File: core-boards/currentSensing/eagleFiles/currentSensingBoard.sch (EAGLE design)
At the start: 22 parts, among them Q1 16MHz

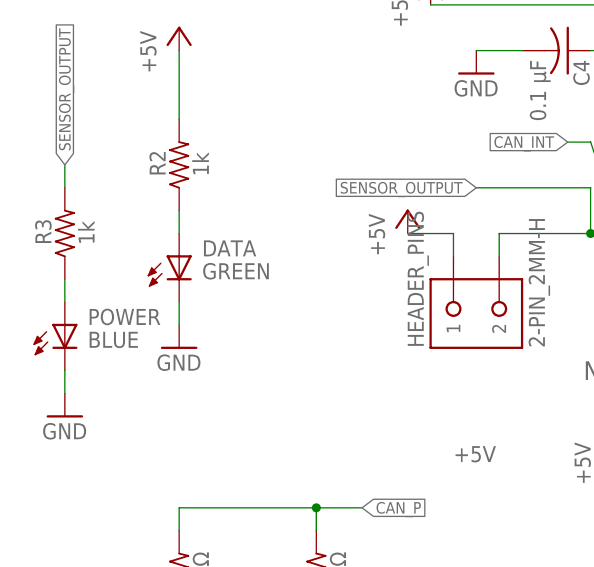
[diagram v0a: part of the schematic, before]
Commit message: Leds fixed
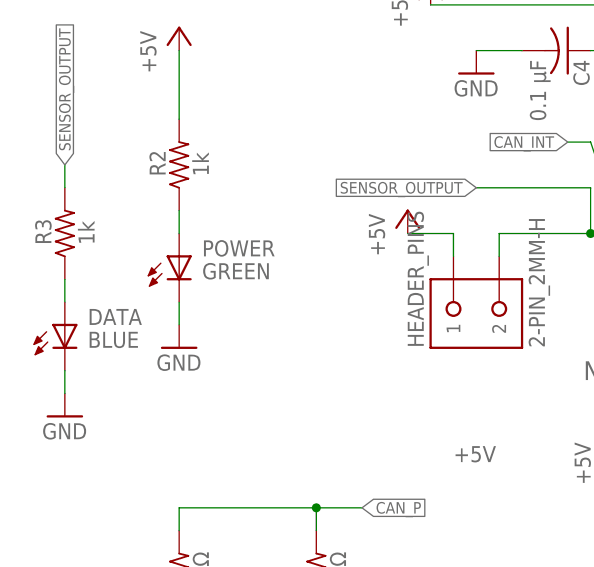
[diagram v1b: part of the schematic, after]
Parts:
- DATA: value GREEN -> BLUE; device RoboJackets-LEDs:LED-SMD-GREEN -> RoboJackets-LEDs:LED-SMD-BLUE
- POWER: value BLUE -> GREEN; device RoboJackets-LEDs:LED-SMD-BLUE -> RoboJackets-LEDs:LED-SMD-GREEN
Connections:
- net N$2: now also DATA.A; no longer POWER.A
- net N$7: now also POWER.A; no longer DATA.A
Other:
- moved on the sheet: DATA, POWER
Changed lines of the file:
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@@
 <part name="P+10" library="supply1" library_urn="urn:adsk.eagle:library:371" deviceset="+5V" device=""/>
 <part name="HEADER_PINS" library="RoboJackets-Connectors" deviceset="2-PIN_2MM-*" device="H"/>
-<part name="DATA" library="RoboJackets-LEDs" deviceset="LED-SMD" device="" technology="-GREEN" value="GREEN"/>
-<part name="POWER" library="RoboJackets-LEDs" deviceset="LED-SMD" device="" technology="-BLUE" value="BLUE"/>
+<part name="POWER" library="RoboJackets-LEDs" deviceset="LED-SMD" device="" technology="-GREEN" value="GREEN"/>
+<part name="DATA" library="RoboJackets-LEDs" deviceset="LED-SMD" device="" technology="-BLUE" value="BLUE"/>
 </parts>
 <sheets>
@@
 <attribute name="VALUE" x="58.42" y="7.62" size="1.778" layer="96" font="vector" rot="R90"/>
 </instance>
-<instance part="DATA" gate="G$1" x="17.78" y="15.24" smashed="yes">
+<instance part="POWER" gate="G$1" x="17.78" y="15.24" smashed="yes">
 <attribute name="NAME" x="20.32" y="17.78" size="1.778" layer="95"/>
 <attribute name="VALUE" x="20.32" y="15.24" size="1.778" layer="96"/>
 </instance>
-<instance part="POWER" gate="G$1" x="5.08" y="7.62" smashed="yes">
+<instance part="DATA" gate="G$1" x="5.08" y="7.62" smashed="yes">
 <attribute name="NAME" x="7.62" y="10.16" size="1.778" layer="95"/>
 <attribute name="VALUE" x="7.62" y="7.62" size="1.778" layer="96"/>
@@
 <pinref part="GND6" gate="1" pin="GND"/>
 <wire x1="5.08" y1="2.54" x2="5.08" y2="5.08" width="0.1524" layer="91"/>
-<pinref part="POWER" gate="G$1" pin="K"/>
+<pinref part="DATA" gate="G$1" pin="K"/>
 </segment>
 <segment>
@@
 <pinref part="GND9" gate="1" pin="GND"/>
 <wire x1="17.78" y1="12.7" x2="17.78" y2="10.16" width="0.1524" layer="91"/>
-<pinref part="DATA" gate="G$1" pin="K"/>
+<pinref part="POWER" gate="G$1" pin="K"/>
 </segment>
 <segment>
@@
 <pinref part="R2" gate="G$1" pin="1"/>
 <wire x1="17.78" y1="20.32" x2="17.78" y2="22.86" width="0.1524" layer="91"/>
-<pinref part="DATA" gate="G$1" pin="A"/>
+<pinref part="POWER" gate="G$1" pin="A"/>
 </segment>
 </net>
@@
 <net name="N$2" class="0">
 <segment>
-<pinref part="POWER" gate="G$1" pin="A"/>
+<pinref part="DATA" gate="G$1" pin="A"/>
 <pinref part="R3" gate="G$1" pin="1"/>
 <wire x1="5.08" y1="12.7" x2="5.08" y2="15.24" width="0.1524" layer="91"/>

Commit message: Board Review Draft
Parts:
- removed DATA: BLUE, RoboJackets-LEDs:LED-SMD-BLUE
- added DEBUG: RED, RoboJackets-LEDs:LED-SMD-RED
- added OUTPUT: BLUE, RoboJackets-LEDs:LED-SMD-BLUE
- added R1: 1k, rcl:R-US_R0603
- renumbered MICROCONTR to IC_MCU_8BIT
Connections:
- new net DEBUG: IC_MCU_8BIT.PD0(RXD/PCINT16), R1.2
- new net N$1: DEBUG.A, R1.1
- net GND: now also DEBUG.K, OUTPUT.K; no longer DATA.K
- net N$2: now also OUTPUT.A; no longer DATA.A
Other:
- moved on the sheet: POWER, R2, R3, R4, R5

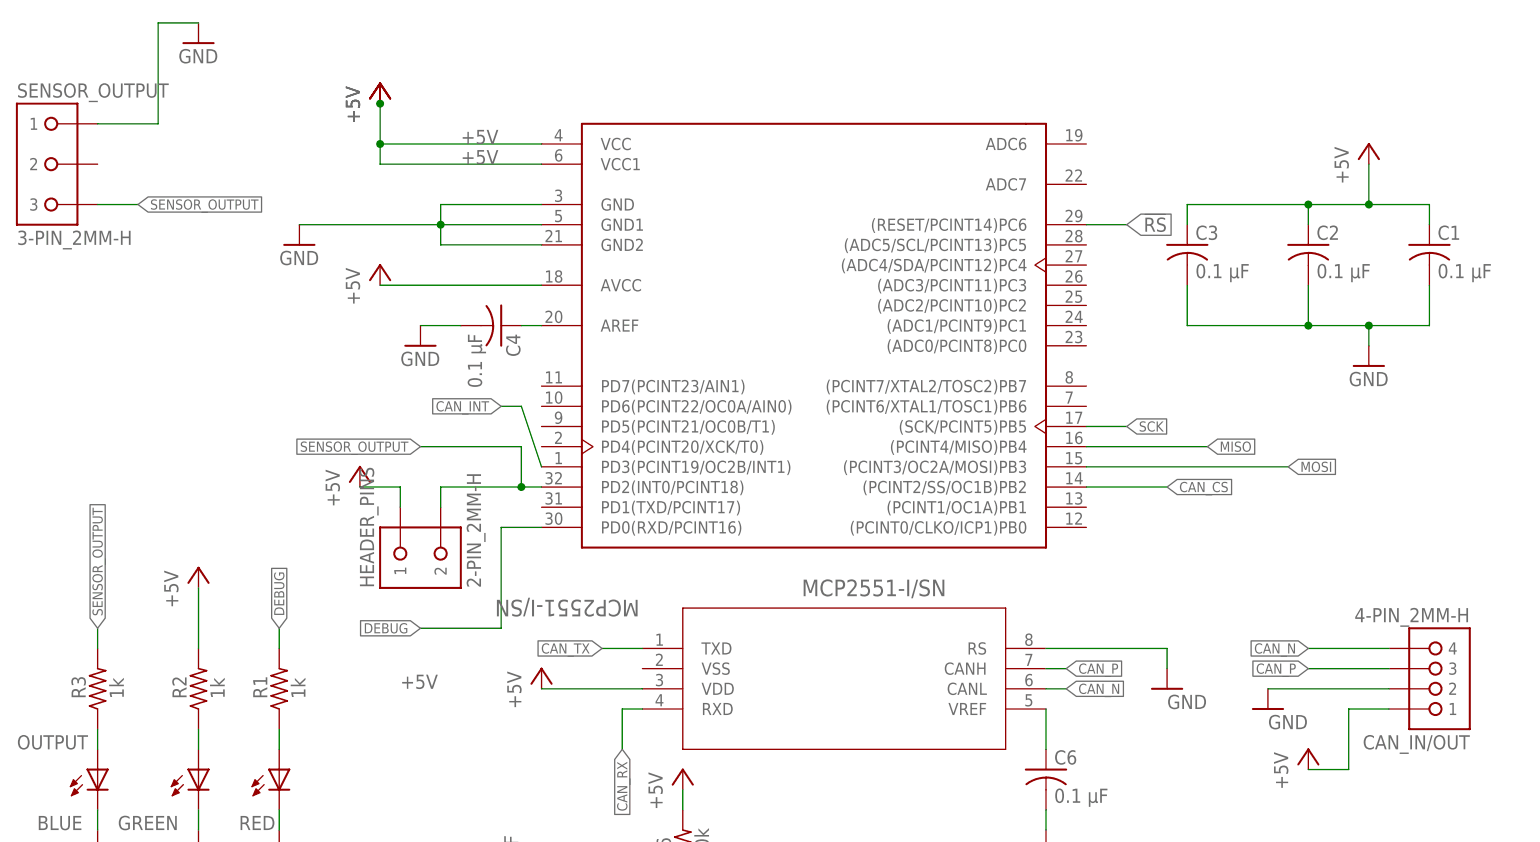
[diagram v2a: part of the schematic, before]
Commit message: Core Edit Current Sensing
Edited from core
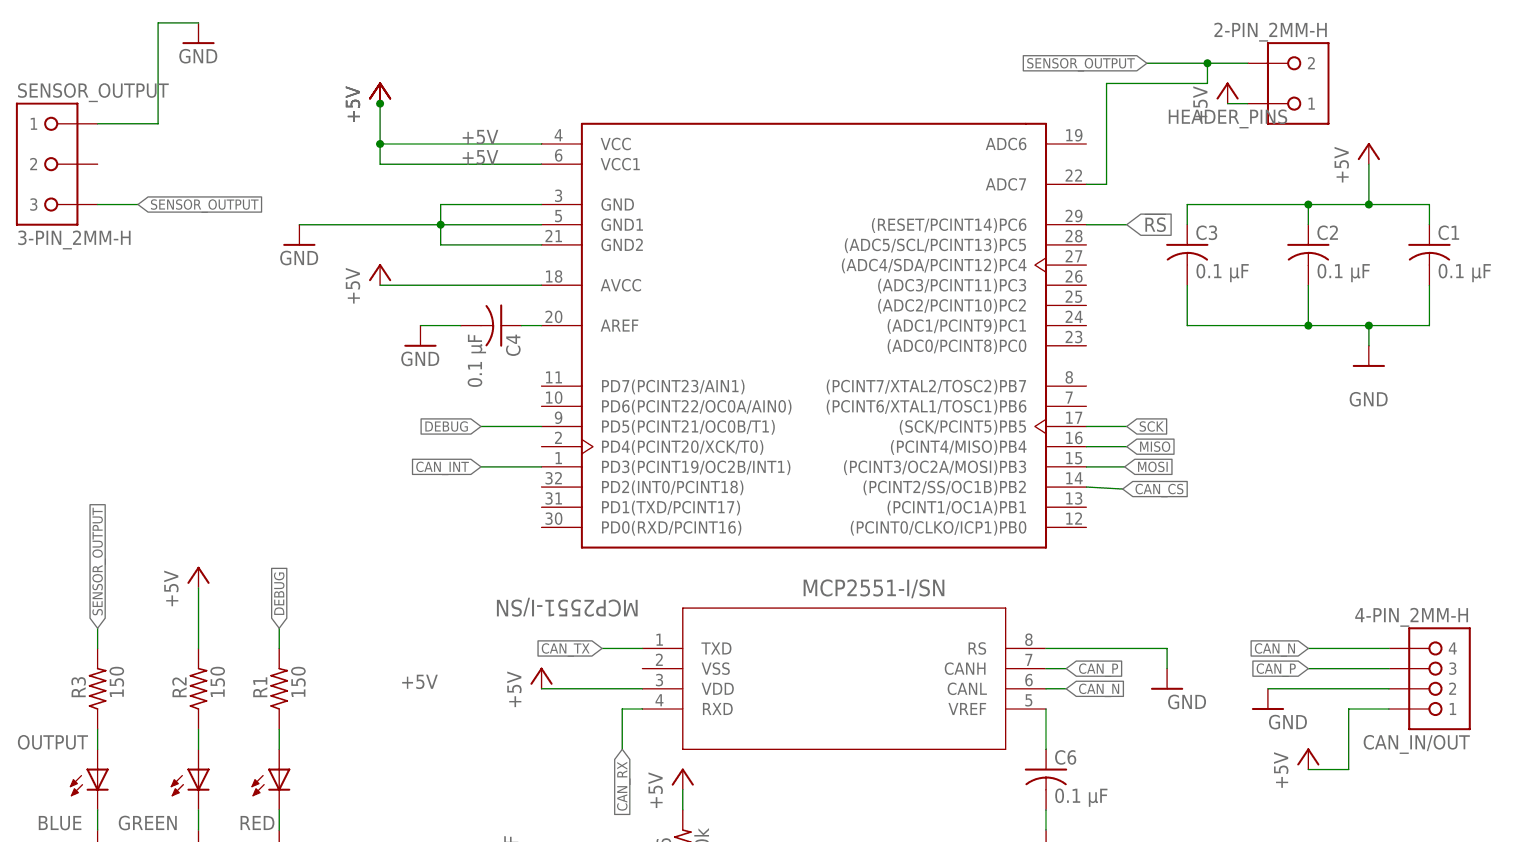
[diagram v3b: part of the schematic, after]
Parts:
- R1, R2, R3: value 1k -> 150
- renumbered IC_MCU_8BIT to TQFP-32(V3)
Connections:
- net DEBUG: now also TQFP-32(V3).PD5(PCINT21/OC0B/T1); no longer TQFP-32(V3).PD0(RXD/PCINT16)
- net SENSOR_OUTPUT: now also TQFP-32(V3).ADC7; no longer TQFP-32(V3).PD2(INT0/PCINT18)
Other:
- moved on the sheet: HEADER_PINS

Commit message: New Updates to Current Sensing
Nearing final stages
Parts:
- removed CAN_IN/OUT: 4-PIN_2MM-H, RoboJackets-Connectors:4-PIN_2MM-H
- removed HEADER_PINS: 2-PIN_2MM-H, RoboJackets-Connectors:2-PIN_2MM-H
- removed OUTPUT: BLUE, RoboJackets-LEDs:LED-SMD-BLUE
- removed R3: 150, rcl:R-US_R0603
- removed SENSOR_OUTPUT: 3-PIN_2MM-H, RoboJackets-Connectors:3-PIN_2MM-H
- removed TQFP-32(V3): ATMEGA328P-AU, Microcontroller:ATMEGA328P-AU
- added ATMEGA328P-AU(V1): ATMEGA328P-AU (V1), Microcontroller:ATMEGA328P-AU
- added X1: 3-PIN_2MM-H, RoboJackets-Connectors:3-PIN_2MM-H
- added X2: 2-PIN_2MM-H, RoboJackets-Connectors:2-PIN_2MM-H
- added X3: 4-PIN_2MM-H, RoboJackets-Connectors:4-PIN_2MM-H
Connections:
- removed net N$2: OUTPUT.A, R3.1
- net !RS: now also ATMEGA328P-AU(V1).(RESET/PCINT14)PC6; no longer TQFP-32(V3).(RESET/PCINT14)PC6
- net +5V: now also ATMEGA328P-AU(V1).AVCC, ATMEGA328P-AU(V1).VCC, ATMEGA328P-AU(V1).VCC1, ICSP-2.S, X2.1, X3.1; no longer CAN_IN/OUT.1, HEADER_PINS.1, TQFP-32(V3).AVCC, TQFP-32(V3).VCC, TQFP-32(V3).VCC1
- net CAN_CS: now also ATMEGA328P-AU(V1).(PCINT2/SS/OC1B)PB2; no longer TQFP-32(V3).(PCINT2/SS/OC1B)PB2
- net CAN_INT: now also ATMEGA328P-AU(V1).PD3(PCINT19/OC2B/INT1); no longer TQFP-32(V3).PD3(PCINT19/OC2B/INT1)
- net CAN_N: now also X3.4; no longer CAN_IN/OUT.4
- net CAN_P: now also X3.3; no longer CAN_IN/OUT.3
- net DEBUG: now also ATMEGA328P-AU(V1).PD5(PCINT21/OC0B/T1); no longer TQFP-32(V3).PD5(PCINT21/OC0B/T1)
- net GND: now also ATMEGA328P-AU(V1).GND, ATMEGA328P-AU(V1).GND1, ATMEGA328P-AU(V1).GND2, ICSP-6.S, X1.1, X3.2; no longer CAN_IN/OUT.2, OUTPUT.K, SENSOR_OUTPUT.1, TQFP-32(V3).GND, TQFP-32(V3).GND1, TQFP-32(V3).GND2
- net MISO: now also ATMEGA328P-AU(V1).(PCINT4/MISO)PB4; no longer TQFP-32(V3).(PCINT4/MISO)PB4
- net MOSI: now also ATMEGA328P-AU(V1).(PCINT3/OC2A/MOSI)PB3, ICSP-4.S; no longer TQFP-32(V3).(PCINT3/OC2A/MOSI)PB3
- net N$6: now also ATMEGA328P-AU(V1).AREF; no longer TQFP-32(V3).AREF
- net SCK: now also ATMEGA328P-AU(V1).(SCK/PCINT5)PB5; no longer TQFP-32(V3).(SCK/PCINT5)PB5
- net SENSOR_OUTPUT: now also ATMEGA328P-AU(V1).ADC7, X1.3, X2.2; no longer HEADER_PINS.2, R3.2, SENSOR_OUTPUT.3, TQFP-32(V3).ADC7
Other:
- note added: "12 volts supplied to AIM Dynamics Current Sensor seperately."
- note added: "CAN Circuit"
- note added: "Header Pins"
- note added: "LEDs"
- note added: "Microcontroller"
- moved on the sheet: C1, C2, C3, C4, C5, C6, C7, DEBUG, ICSP-1, ICSP-2, ICSP-3, ICSP-4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

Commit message: Changes to Board Complete
-Most recent round of commentes taken account of
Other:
- moved on the sheet: C1, C2, C3, C4, C5, C6, C7, DEBUG, ICSP-1, ICSP-2, ICSP-3, ICSP-4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

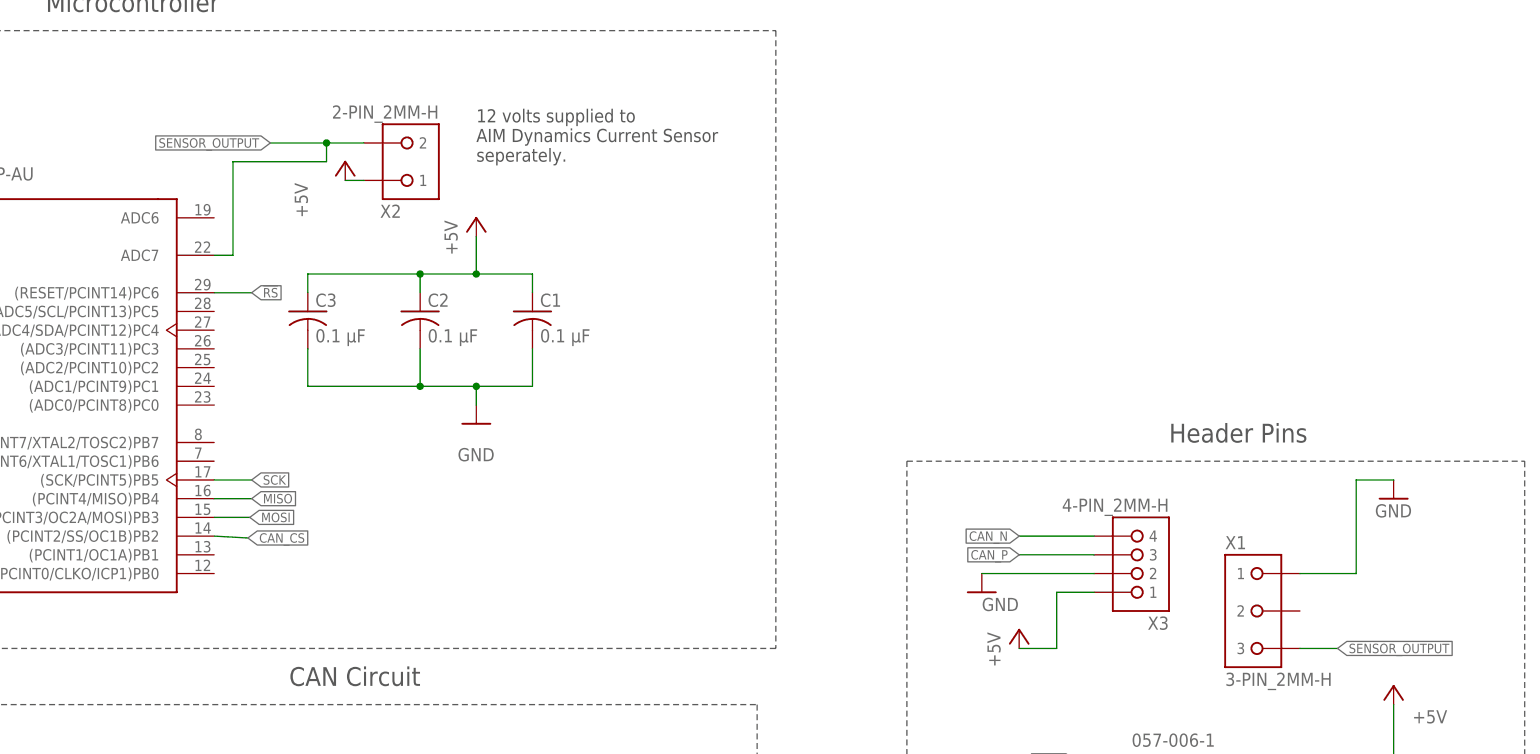
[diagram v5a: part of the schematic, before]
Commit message: Current Sensing with Female resistor input
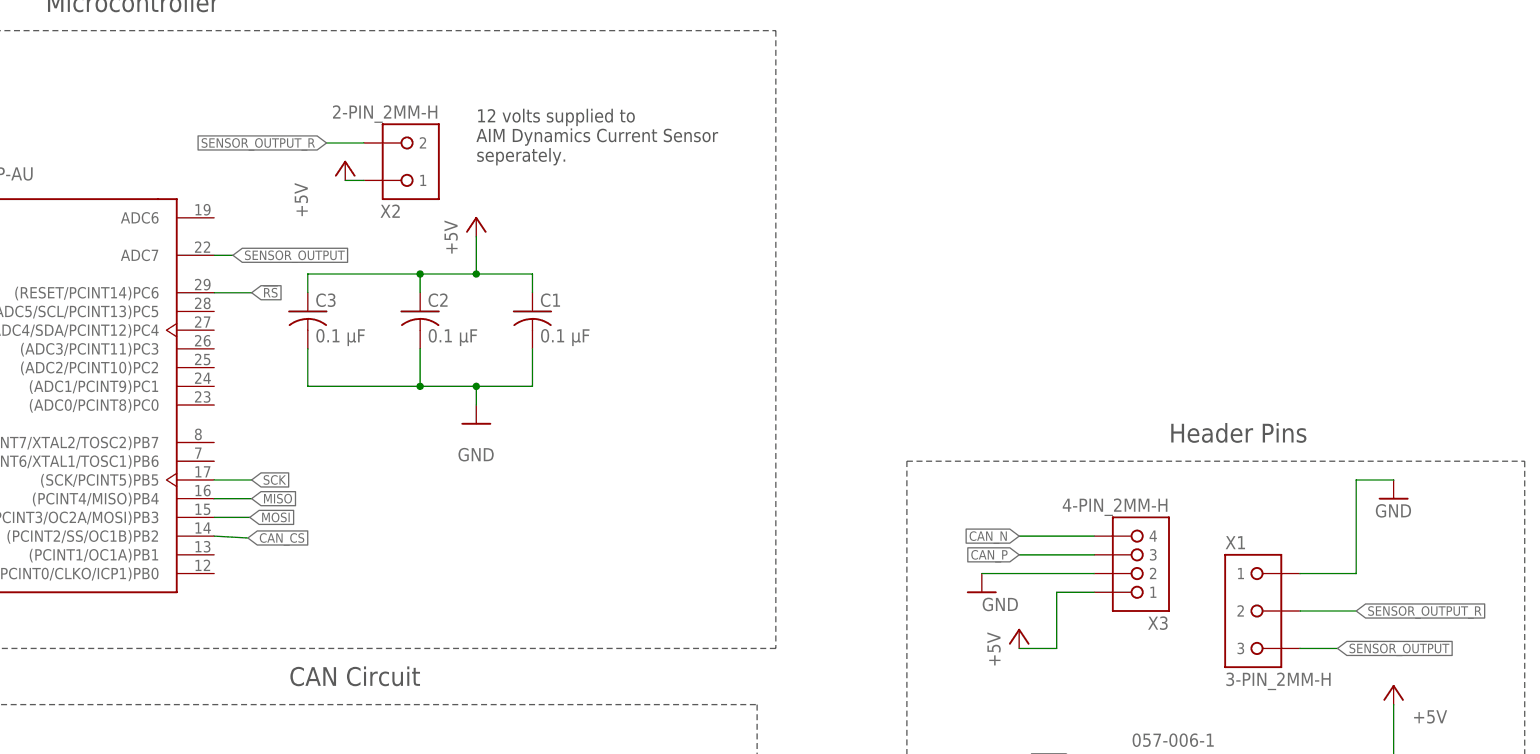
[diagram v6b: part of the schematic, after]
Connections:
- new net SENSOR_OUTPUT_R: X1.2, X2.2
- net SENSOR_OUTPUT: no longer X2.2
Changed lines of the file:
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@@
 </segment>
 <segment>
-<label x="198.12" y="220.98" size="1.27" layer="95" font="vector" rot="R180" xref="yes"/>
-<wire x1="210.82" y1="220.98" x2="205.74" y2="220.98" width="0.1524" layer="91"/>
-<pinref part="X2" gate="G$1" pin="2"/>
-<wire x1="205.74" y1="220.98" x2="198.12" y2="220.98" width="0.1524" layer="91"/>
-<wire x1="193.04" y1="218.44" x2="205.74" y2="218.44" width="0.1524" layer="91"/>
-<wire x1="205.74" y1="218.44" x2="205.74" y2="220.98" width="0.1524" layer="91"/>
-<junction x="205.74" y="220.98"/>
 <pinref part="ATMEGA328P-AU(V1)" gate="G$1" pin="ADC7"/>
-<wire x1="193.04" y1="218.44" x2="193.04" y2="205.74" width="0.1524" layer="91"/>
 <wire x1="193.04" y1="205.74" x2="190.5" y2="205.74" width="0.1524" layer="91"/>
+<label x="193.04" y="205.74" size="1.27" layer="95" xref="yes"/>
 </segment>
 </net>
@@
 </segment>
 </net>
+<net name="SENSOR_OUTPUT_R" class="0">
+<segment>
+<pinref part="X2" gate="G$1" pin="2"/>
+<wire x1="210.82" y1="220.98" x2="205.74" y2="220.98" width="0.1524" layer="91"/>
+<label x="205.74" y="220.98" size="1.27" layer="95" rot="R180" xref="yes"/>
+</segment>
+<segment>
+<pinref part="X1" gate="G$1" pin="2"/>
+<wire x1="337.82" y1="157.48" x2="345.44" y2="157.48" width="0.1524" layer="91"/>
+<label x="345.44" y="157.48" size="1.27" layer="95" xref="yes"/>
+</segment>
+</net>
